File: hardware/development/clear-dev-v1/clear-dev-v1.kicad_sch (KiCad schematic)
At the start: 77 parts, among them J1 USB_B_Micro, J10 Conn_01x28_Pin, J11 Conn_01x28_Pin, J2 Conn_01x02_Pin, J3 Conn_01x02_Pin, J4 Conn_01x03_Pin, J5 Conn_01x02_Pin, J6 Conn_01x02_Pin, J7 Conn_01x06_Pin, J8 Conn_01x02_Pin, J9 Conn_01x02_Pin, SW1 SW_Push - SKQGADE010, T1 Logo, T2 Logo, U1 FT232H, U10 DS1086LU, U2 SN74LVC1G125DCKR, U3 SN74LVC1G125DCKR, U5 TAR5SxxU, U6 TAR5SxxU, U7 W25Q32FVSS, U8 M.2-CONNECTOR-E, U9 TMUX4053-BQB, X1 DSC6001_10MHZ, Y1 12MHz

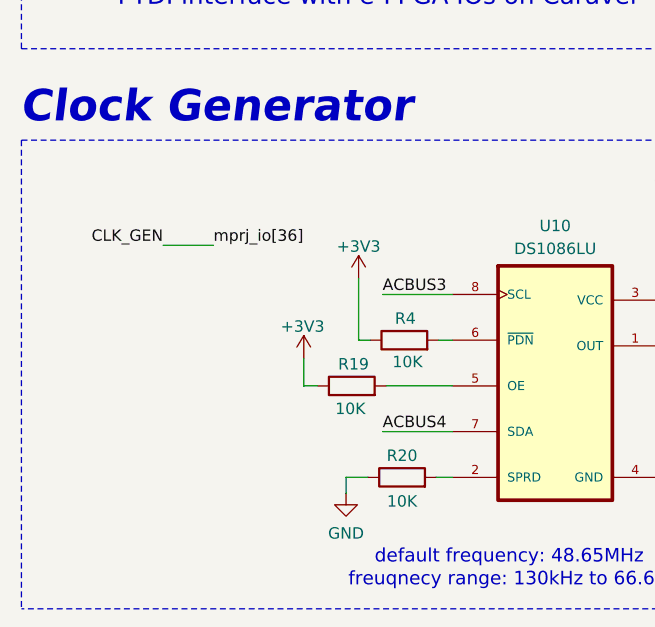
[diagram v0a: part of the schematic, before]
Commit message: ~ update clear PCB with test pads for clock generator dither enable and power-down mode enable to allow enabling them if needed
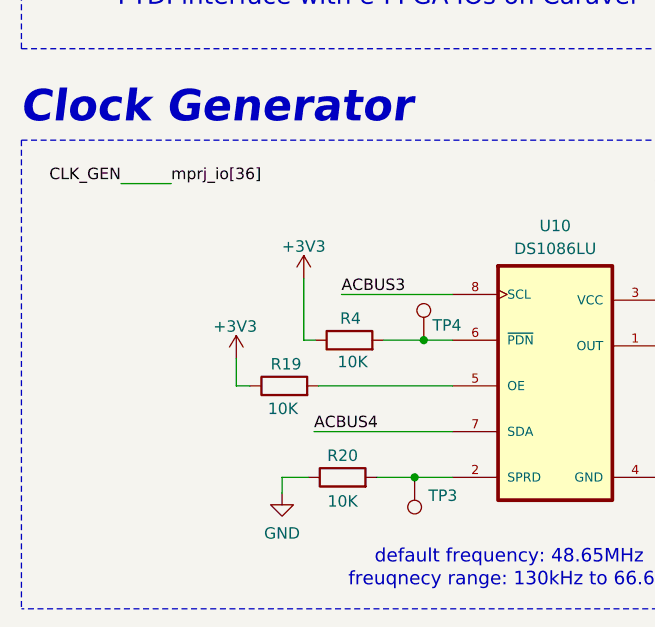
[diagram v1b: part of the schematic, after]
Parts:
- added TP3, TP4: TestPoint, TestPoint:TestPoint_Pad_1.5x1.5mm, symbol Connector:TestPoint
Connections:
- net at R20.2, U10.2 (SPRD): now also TP3.1
- net at R4.2, U10.6 (~{PDN}): now also TP4.1
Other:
- moved on the sheet: R19, R20, R4

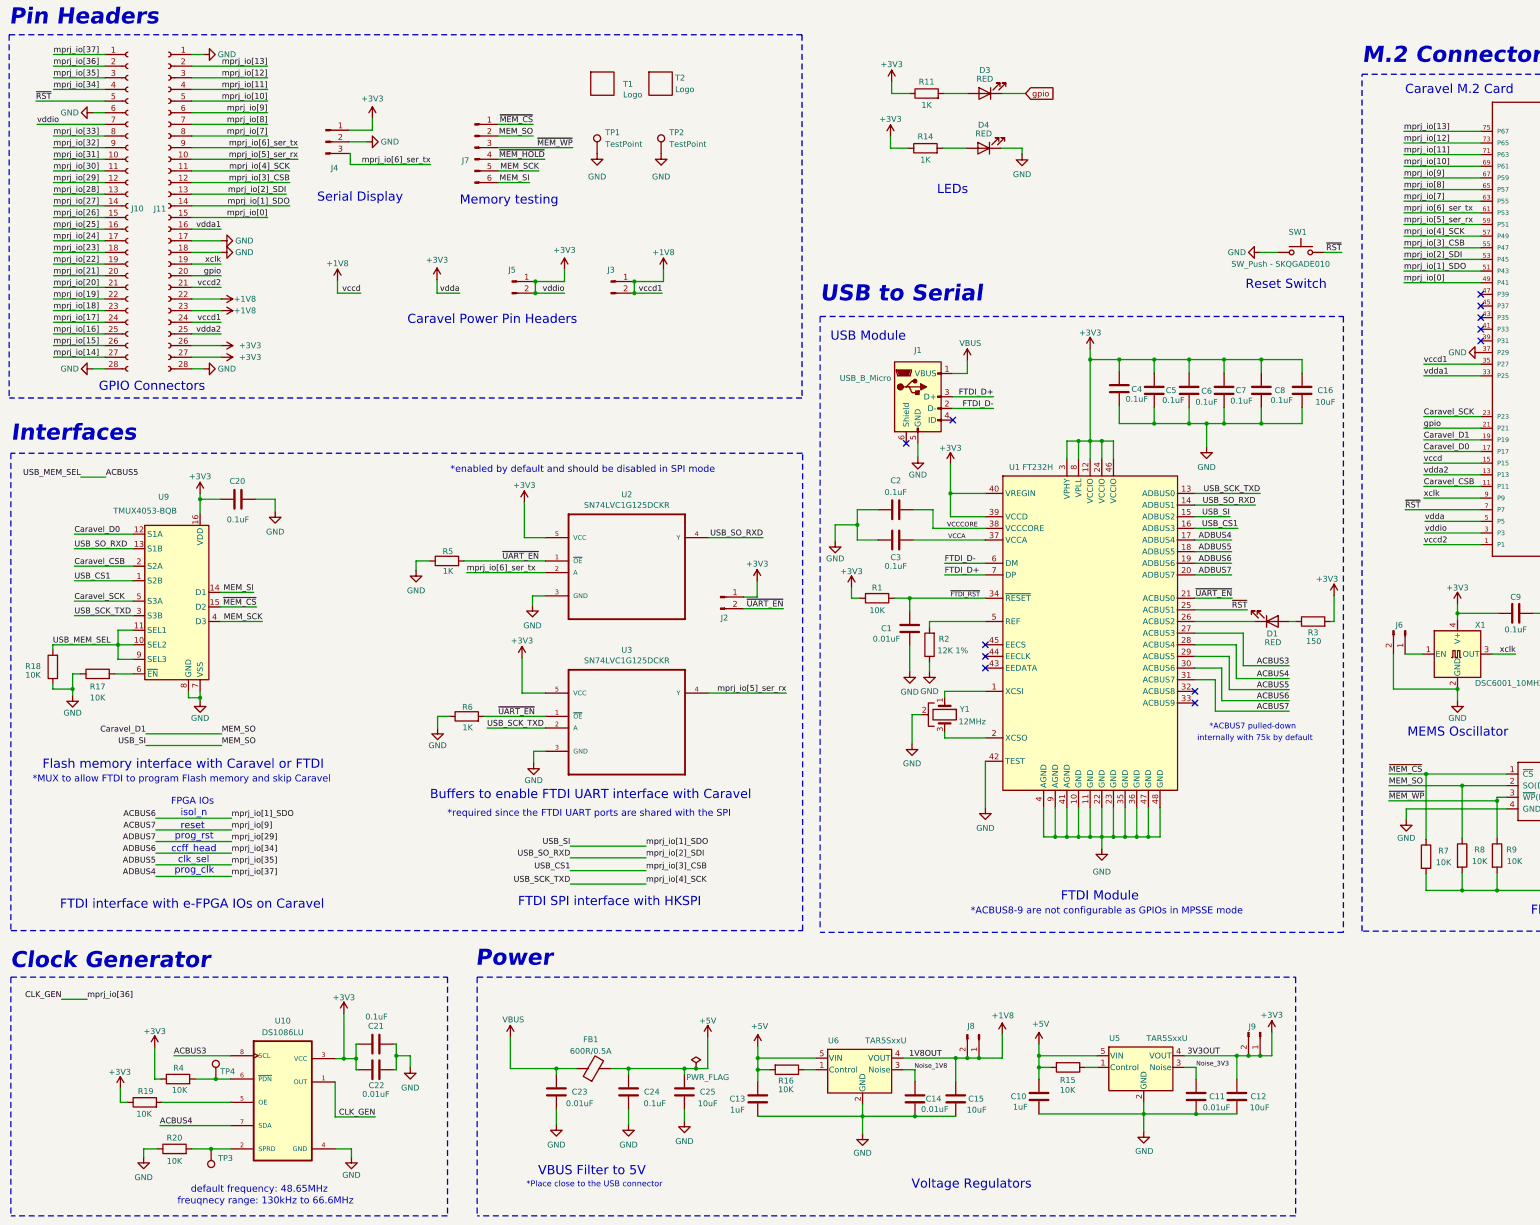
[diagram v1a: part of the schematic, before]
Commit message: + add a tri-state buffer to connect `MEM_SO` to `USB_SI` only when the FTDI is programming the Flash
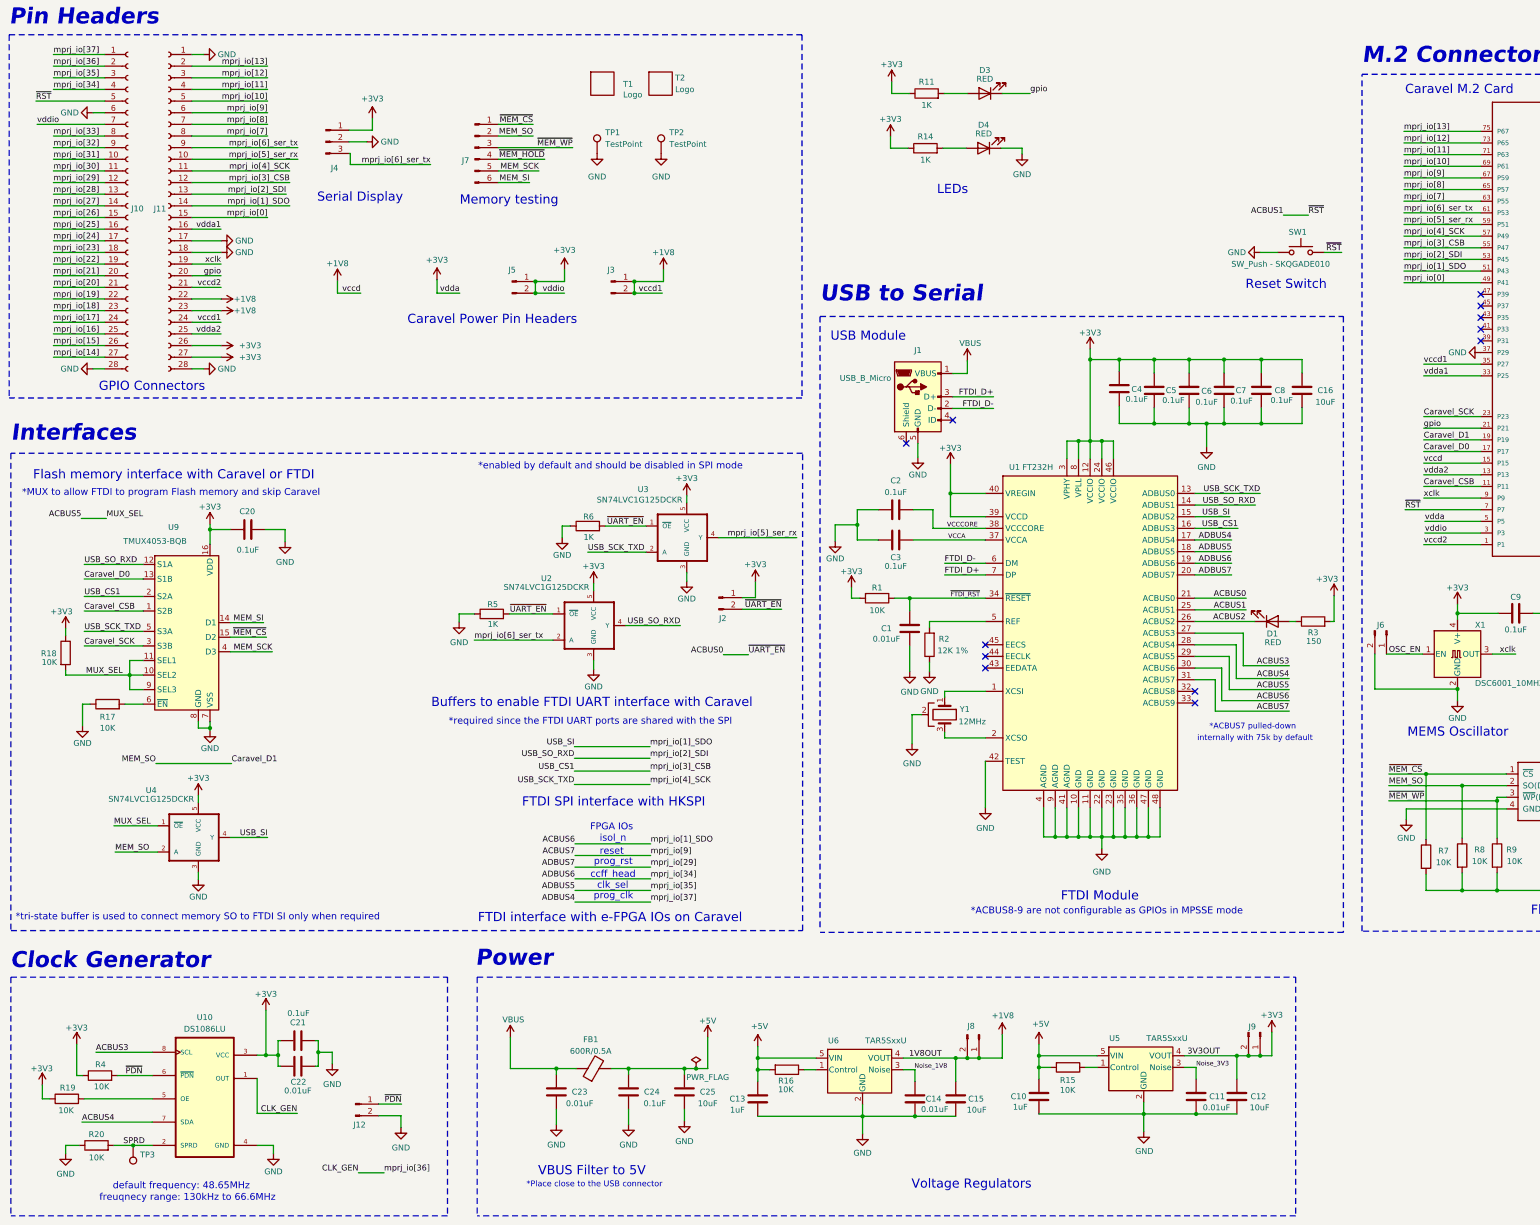
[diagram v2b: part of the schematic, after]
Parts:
- removed TP4: TestPoint, TestPoint:TestPoint_Pad_1.5x1.5mm, symbol Connector:TestPoint
- added J12: Conn_01x02_Pin, Connector_PinHeader_2.54mm:PinHeader_1x02_P2.54mm_Vertical, symbol Connector:Conn_01x02_Pin
- added U4: SN74LVC1G125DCKR, SOT65P210X110-5N, symbol Caravel_board:SN74LVC1G125DCKR
- TP3: footprint TestPoint:TestPoint_Pad_1.5x1.5mm -> TestPoint:TestPoint_THTPad_2.0x2.0mm_Drill1.0mm
- U2, U3: footprint strive_foot_prints:SOT65P210X110-5N -> SOT65P210X110-5N; Field4 (none) -> 76C4082; Field5 (none) -> Texas Instruments; Field6 (none) -> SN74LVC1G125DCKR; Field7 (none) -> 1470771
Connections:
- net +3V3: now also R18.1, U4.5 (VCC)
- net ACBUS5: now also U4.1 (~{OE})
- net ACBUS6: now also U4.4 (Y); no longer J7.2 (Pin_2), R8.1, U7.2 (SO(D1)), U8.19 (P19)
- net Caravel_CSB: now also U9.1 (S2B); no longer U9.2 (S2A)
- net Caravel_D0: now also U9.13 (S1B); no longer U9.12 (S1A)
- net Caravel_SCK: now also U9.3 (S3B); no longer U9.5 (S3A)
- net GND: now also J12.2 (Pin_2), U4.3 (GND); no longer R18.1
- net USB_CS1: now also U9.2 (S2A); no longer U9.1 (S2B)
- net USB_SCK_TXD: now also U9.5 (S3A); no longer U9.3 (S3B)
- net USB_SO_RXD: now also U9.12 (S1A); no longer U9.13 (S1B)
- net OSC_EN: now reaches J6.1 (Pin_1), X1.1 (EN)
- net ACBUS2: now reaches D1.1 (K), U1.26 (ACBUS2)
- net ~{PDN}: now reaches R4.2, U10.6 (~{PDN})
- net ~{PDN}: now also J12.1 (Pin_1)
- net SPRD: now reaches R20.2, TP3.1, U10.2 (SPRD)
- net ~{RST} renamed ACBUS1
- net ~{UART_EN} renamed ACBUS0
- new net Caravel_D1: J7.2 (Pin_2), R8.1, U4.2 (A), U7.2 (SO(D1)), U8.19 (P19)
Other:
- note added: "*tri-state buffer is used to connect memory SO to FTDI SI only when required"
- moved on the sheet: C20, C21, C22, J6, R17, R18, R19, R20, R4, R5, R6, TP3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

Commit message: ~ update clear dev pcb
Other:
- company: (none) -> Efabless
- title: (none) -> Clear Chip Development Board
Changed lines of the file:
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@@
 (kicad_sch (version 20230121) (generator eeschema)
   (paper "A3")
+  (title_block
+    (title "Clear Chip Development Board")
+    (rev "REV 1A")
+    (company "Efabless")
+  )
   (junction (at 260.731 196.596) (diameter 0) (color 0 0 0 0)
   )

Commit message: update clear dev board to REV 1B
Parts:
- added JP1, JP2, JP3, JP4, JP5, JP6: SolderJumper_2_Bridged, SolderJumper-2_P1.3mm_Bridged_Pad1.0x1.5mm, symbol Jumper:SolderJumper_2_Bridged
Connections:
- net +3V3: now also J10.3 (Pin_3); no longer C20.2, J10.7 (Pin_7), U9.16 (VDD)
- net +5V: now also C20.2, U9.16 (VDD)
- net ACBUS1: now also J10.1 (Pin_1); no longer J10.5 (Pin_5)
- net ACBUS6: now also JP1.1 (A)
- net ACBUS7: now also JP2.1 (A)
- net ADBUS4: now also J10.4 (Pin_4), JP6.1 (A); no longer J10.1 (Pin_1)
- net ADBUS5: now also J10.6 (Pin_6), JP5.1 (A); no longer J10.3 (Pin_3)
- net ADBUS6: now also J10.7 (Pin_7), JP4.1 (A); no longer J10.4 (Pin_4)
- net ADBUS7: now also JP3.1 (A)
- net CLK_GEN: now also J10.5 (Pin_5); no longer J10.2 (Pin_2)
- net GND: now also J10.2 (Pin_2); no longer J10.6 (Pin_6)
- net mprj_io[17]: now also JP1.2 (B)
- net mprj_io[18]: now also JP2.2 (B)
- net mprj_io[19]: now also JP3.2 (B)
- net mprj_io[20]: now also JP4.2 (B)
- net mprj_io[21]: now also JP5.2 (B)
- net mprj_io[24]: now also JP6.2 (B)
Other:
- note added: "Clear REV 1B"
- note added: "FTDI and Caravel IOs interfaces with e-FPGA IOs on Caravel"
- note removed: "FTDI interface with e-FPGA IOs on Caravel"
- moved on the sheet: D3, D4, R11, R14, R5, R6, U2, U3
